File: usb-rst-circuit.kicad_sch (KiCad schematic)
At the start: 24 parts, among them J3 USB, Q1 MMBT3904, Q5 MMBT3904, Q6 MMBT3904, SW2 BTN_RST, SW3 BTN_BOOT, U2 USBLC6-2SC6

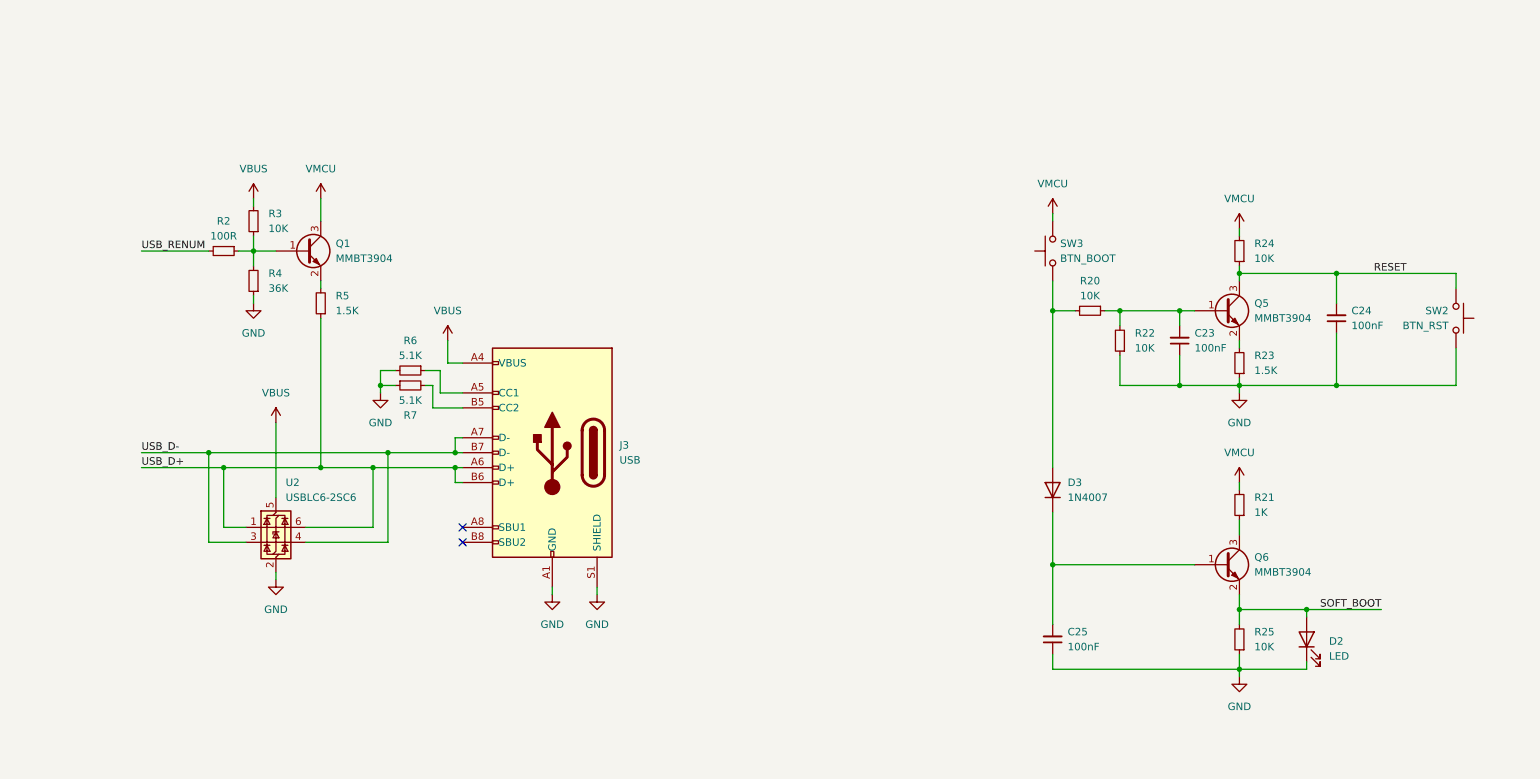
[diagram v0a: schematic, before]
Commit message: Added footwitch, usb led activity
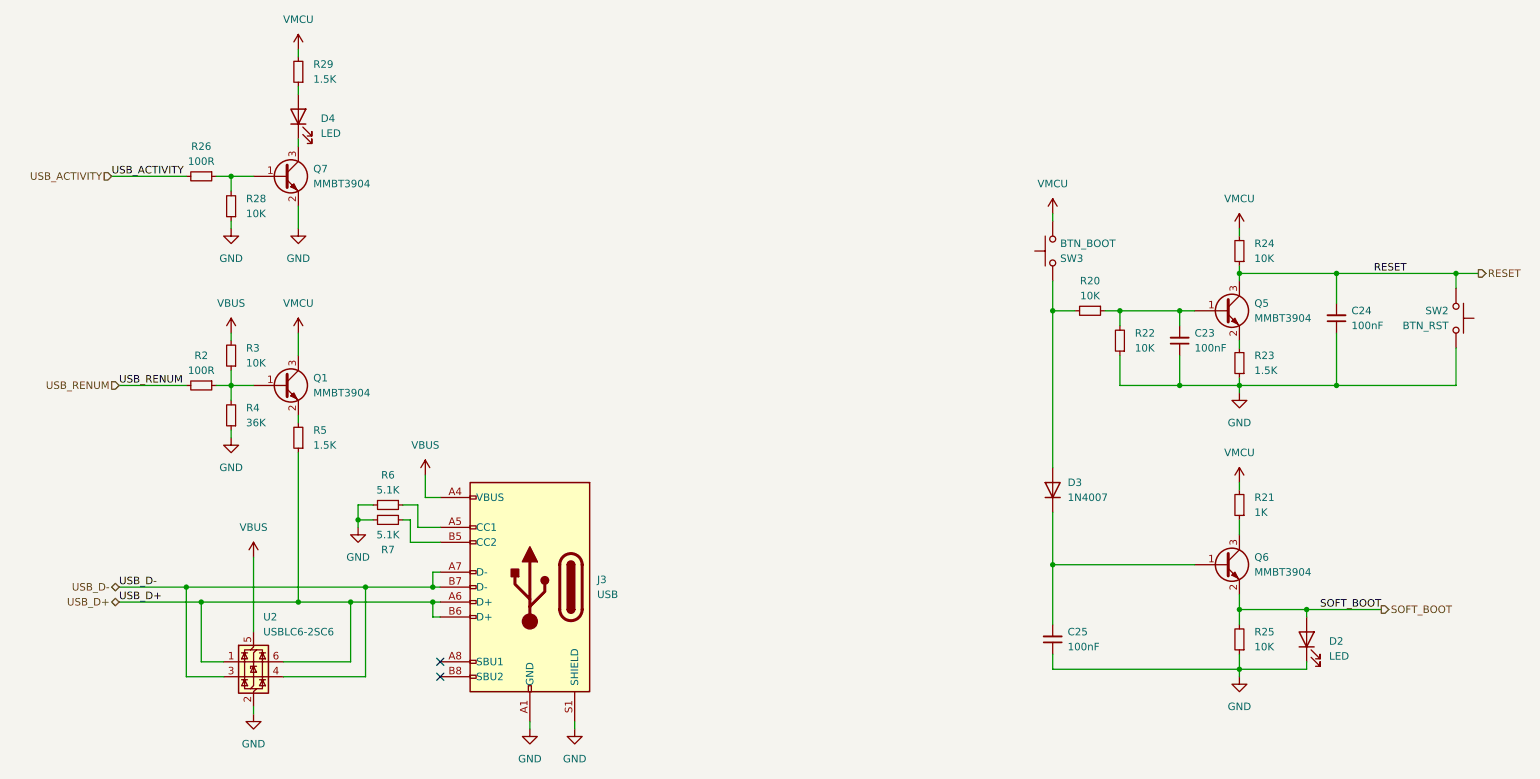
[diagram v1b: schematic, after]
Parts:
- added D4: LED, LED_THT:LED_D3.0mm_Horizontal_O1.27mm_Z2.0mm, symbol Device:LED
- added Q7: MMBT3904, Package_TO_SOT_SMD:SOT-23, symbol Transistor_BJT:MMBT3904
- added R26: 100R, Resistor_SMD:R_0603_1608Metric, symbol Device:R_Small
- added R28: 10K, Resistor_SMD:R_0603_1608Metric, symbol Device:R_Small
- added R29: 1.5K, Resistor_SMD:R_0603_1608Metric, symbol Device:R_Small
- SW3: footprint Button_Switch_THT:SW_PUSH_6mm_H5mm -> Button_Switch_THT:SW_Tactile_SPST_Angled_PTS645Vx83-2LFS
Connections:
- net GND: now also Q7.2 (E), R28.1
- net VMCU: now also SW3.1, R29.2; no longer SW3.2
- net at D3.2 (A), R20.2: now also SW3.2; no longer SW3.1
- new net: D4.1 (K), Q7.3 (C)
- new net: D4.2 (A), R29.1
- new net: Q7.1 (B), R26.1, R28.2
- new net USB_ACTIVITY: R26.2
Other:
- moved on the sheet: J3, Q1, R2, R3, R4, R5, R6, R7, U2
